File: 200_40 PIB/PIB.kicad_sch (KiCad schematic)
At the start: 160 parts, among them J1 M80-5100442, J11 53398-0271, J12 M80-5100842, J13 53398-0271, J15 53398-0571, J2 53398-0471, J3 G125-MS12605M2P, J5 53398-1371, J6 MMCX, J8 SWD/DEBUG, Q1 Si7489DP, Q11 IRF7832, Q2 Si7489DP, Q9 IRF7832, SW1 B3F-1000, U10 LT8580EDD, U12 MAX823TEUK_T, U14 74HC08PW, U15 74HC08PW, U4 STM32G431RBTx, U5 ADM1270ACPZ, U7 ADM1270ACPZ, Y1 ABM3B-8.000MHZ-10-D1G-T

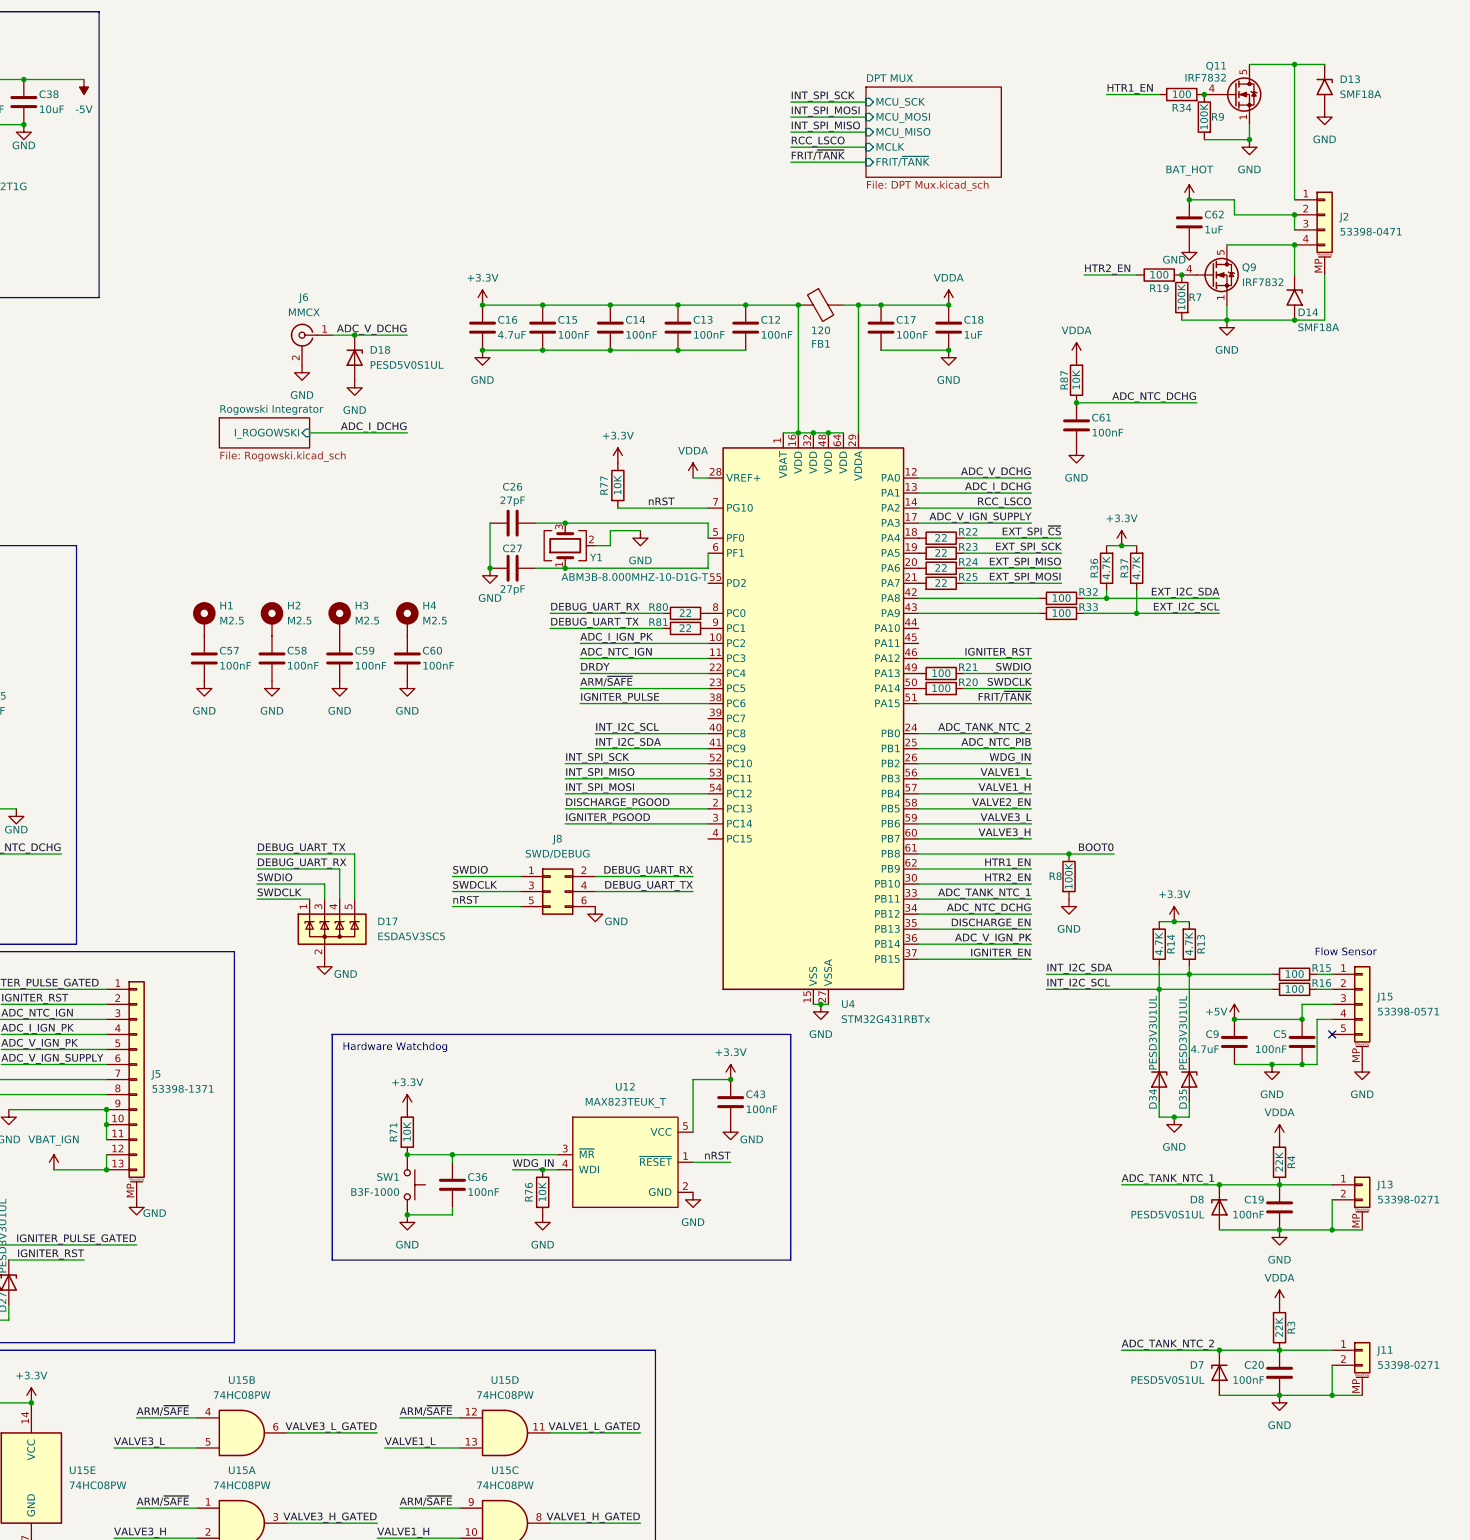
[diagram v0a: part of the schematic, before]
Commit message: clean up schematic
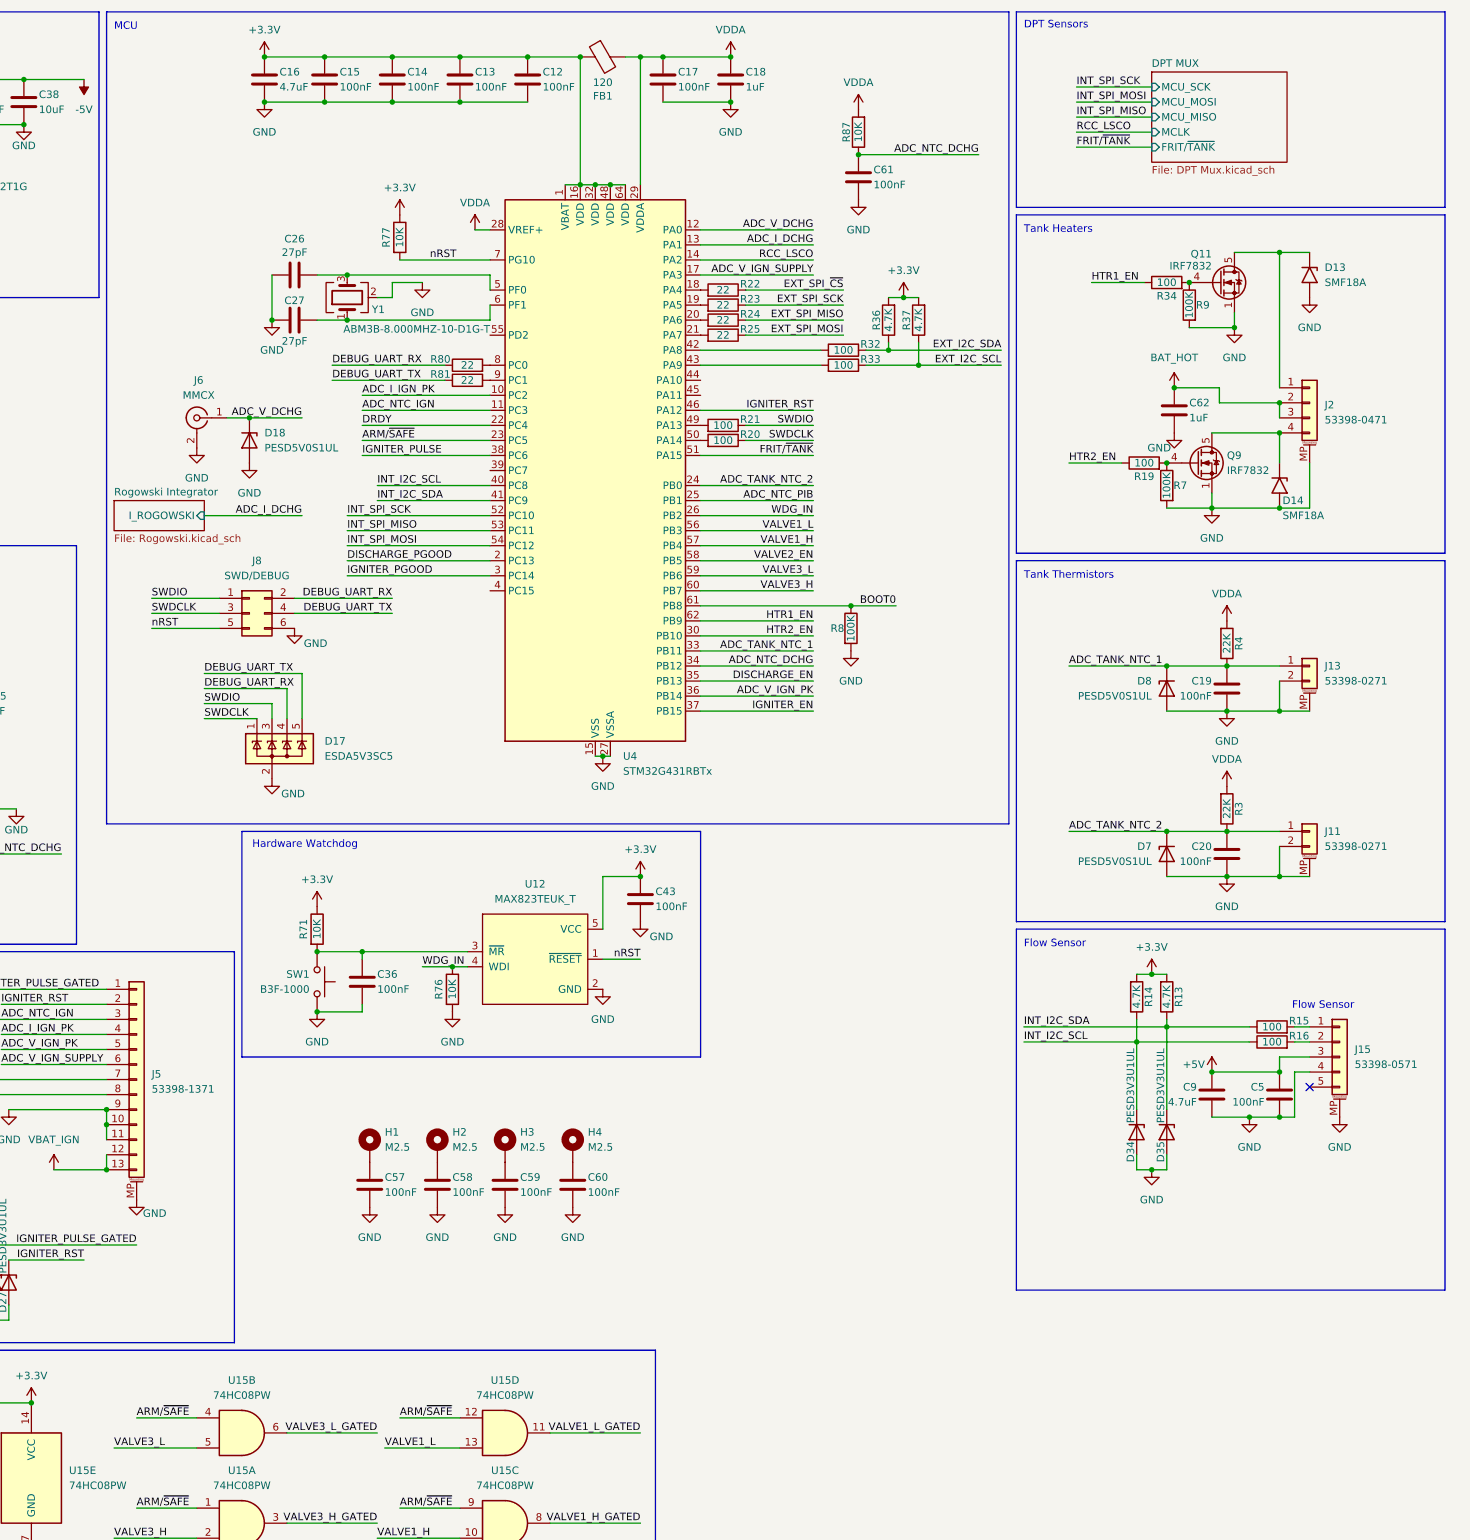
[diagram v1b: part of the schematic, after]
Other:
- note added: "DPT Sensors"
- note added: "MCU"
- note added: "Tank Heaters"
- note added: "Tank Thermistors"
- moved on the sheet: C12, C13, C14, C15, C16, C17, C18, C19, C20, C26, C27, C36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

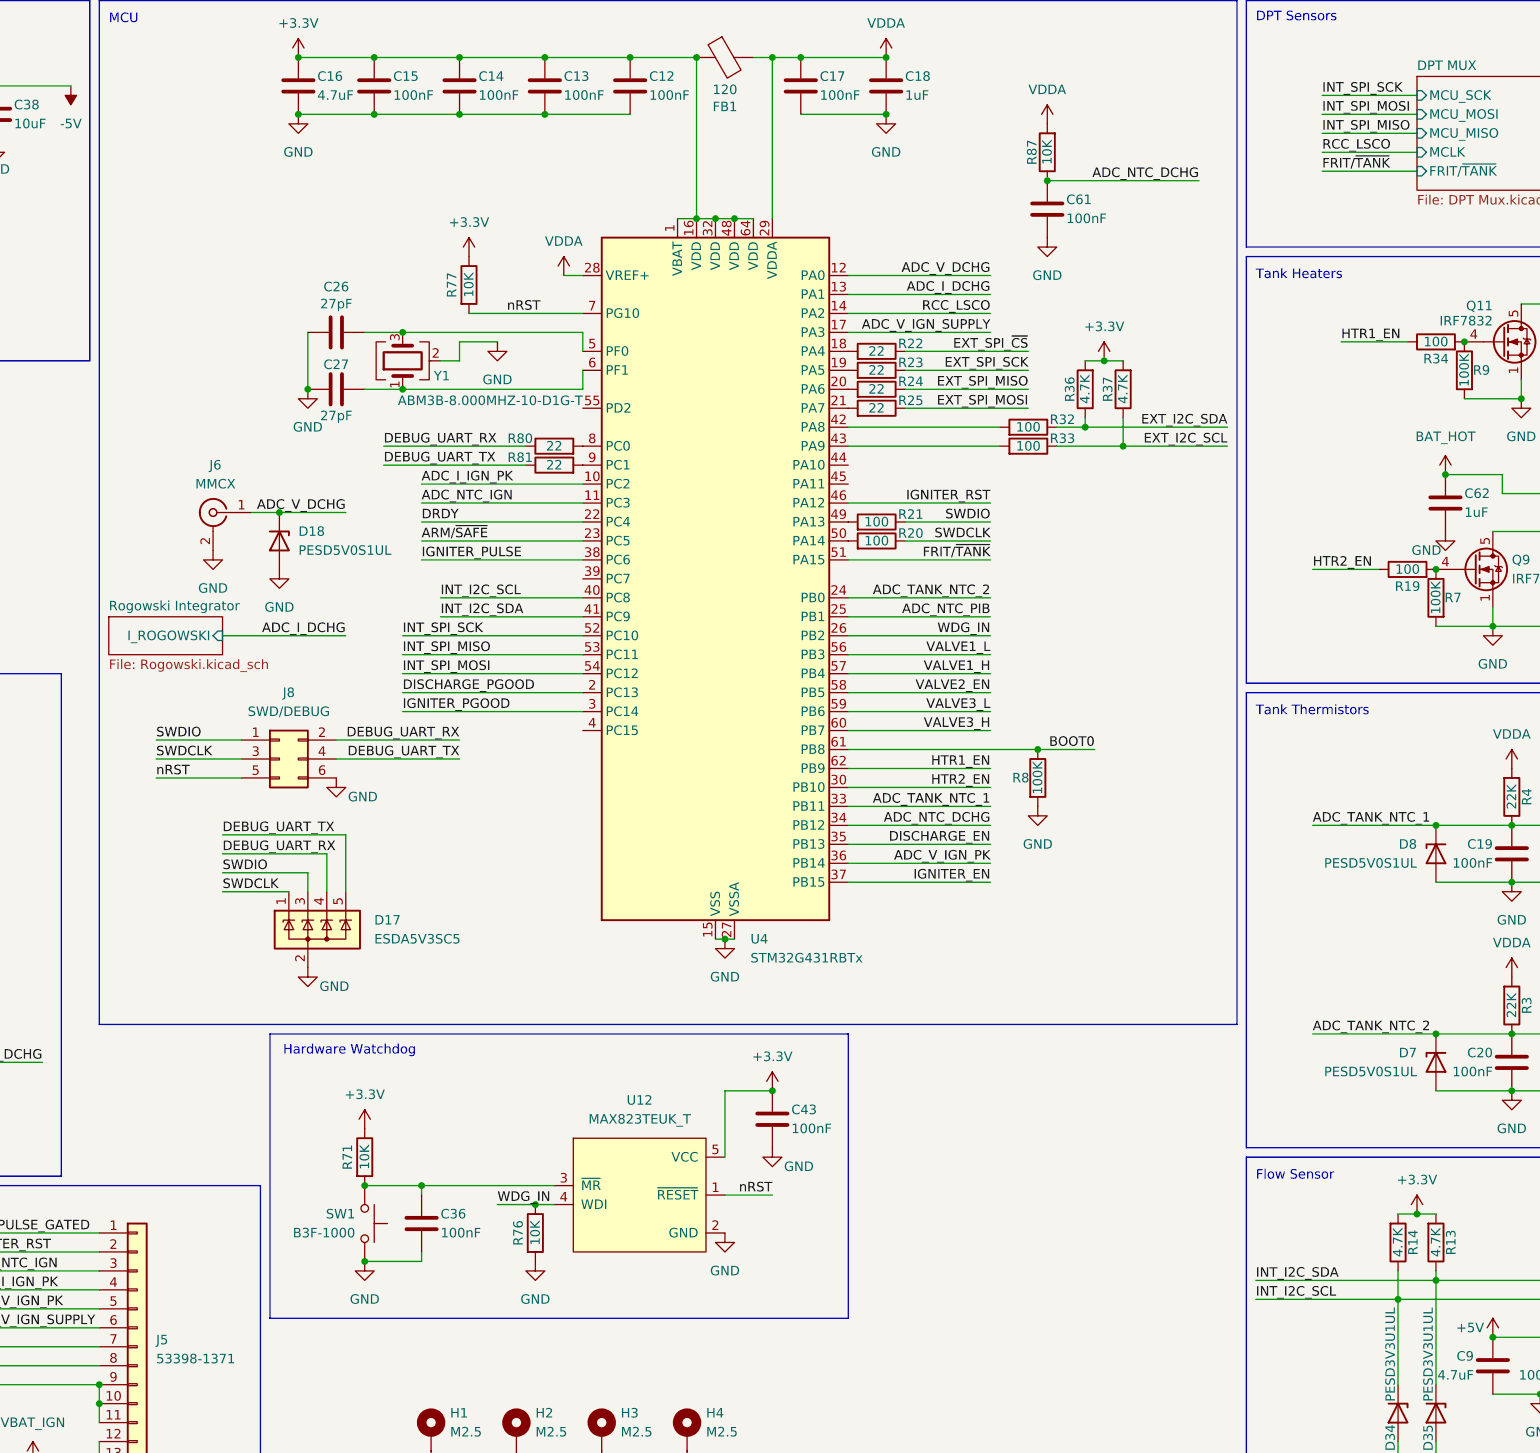
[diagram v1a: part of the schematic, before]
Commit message: fix GSE valve having no power path, fix arm/safe gate floating on reset, fix resistor OR on GSE NC valve, add NC valve flyback diode, change DPT MCLK source to a timer off of HSE, fix crystal load capacitances
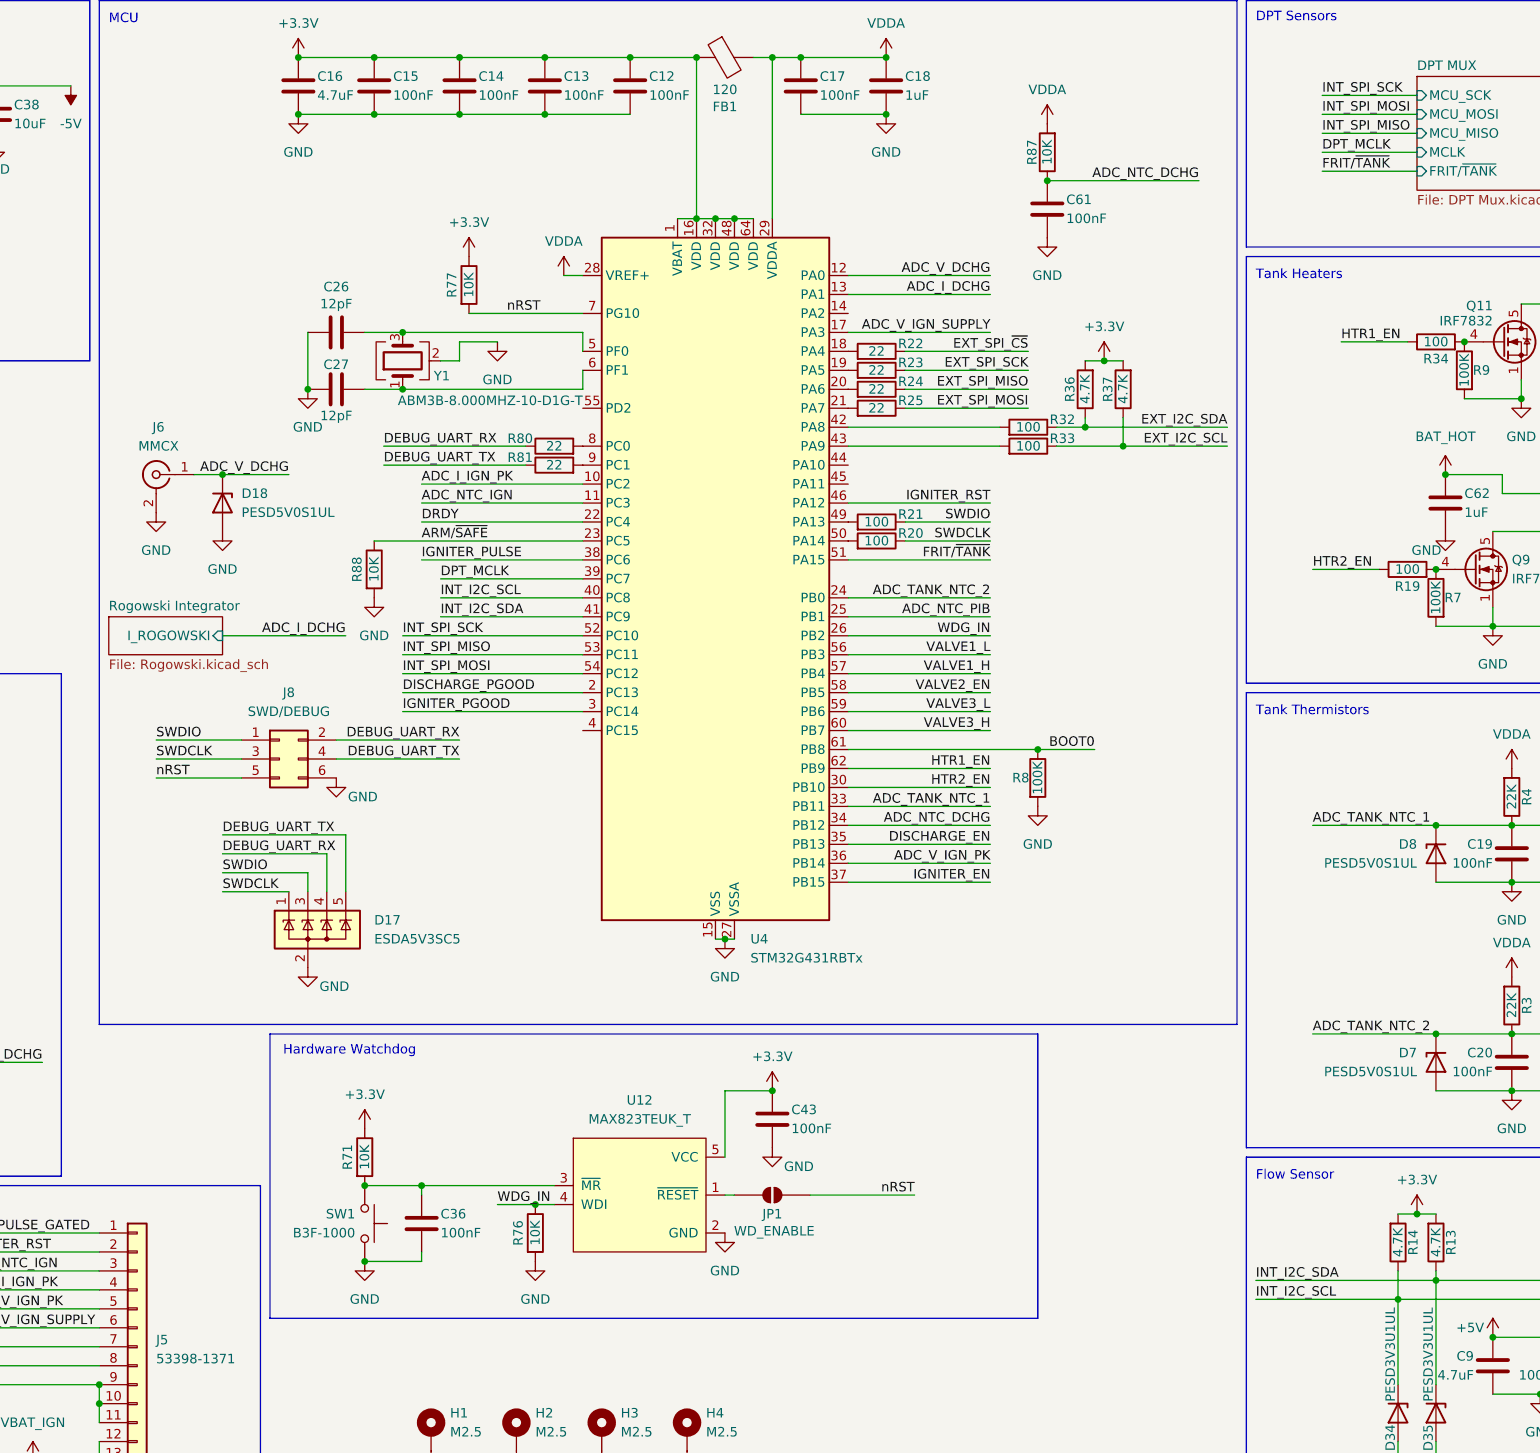
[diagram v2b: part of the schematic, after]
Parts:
- added JP1: WD_ENABLE, Jumper:SolderJumper-2_P1.3mm_Open_Pad1.0x1.5mm, symbol Jumper:SolderJumper_2_Open
- added R88: 10K, Resistor_SMD:R_0402_1005Metric, symbol Device:R
- C26, C27: value 27pF -> 12pF
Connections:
- net ARM/~{SAFE}: now also R88.1
- net GND: now also R88.2
- net nRST: now also JP1.2 (B); no longer U12.1 (~{RESET})
- net DPT_MCLK: now reaches U4.39 (PC7)
- net RCC_LSCO: no longer names the net of U4.14 (PA2)
- new net: JP1.1 (A), U12.1 (~{RESET})
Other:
- moved on the sheet: D18, J6

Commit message: clear out claude flagged items
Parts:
- removed D18: PESD5V0S1UL, Diode_SMD:D_SOD-882, symbol Diode:PESD5V0S1UL
- removed J6: MMCX, Connector_Coaxial:MMCX_Molex_73415-1471_Vertical, symbol Connector:Conn_Coaxial
- added C76, C77: 100nF, Capacitor_SMD:C_0402_1005Metric, symbol Device:C
- added D18: LED, LED_SMD:LED_0603_1608Metric, symbol Device:LED
- added D45, D46, D49: PESD3V3U1UL, Diode_SMD:D_SOD-882, symbol Diode:PESD3V3U1UL
- added R103, R108: 1K, Resistor_SMD:R_0402_1005Metric, symbol Device:R
- added R109: 10K, Resistor_SMD:R_0402_1005Metric, symbol Device:R
- added TH1: 3435K 10K, Resistor_SMD:R_0603_1608Metric, symbol Device:Thermistor_NTC
- added U8: 74AHC1G125, Package_TO_SOT_SMD:SOT-23-5, symbol 74xGxx:74AHC1G125
- SW1: value B3F-1000 -> SKRKAHE020; footprint Button_Switch_THT:SW_PUSH_6mm -> Button_Switch_SMD:SW_Push_SPST_NO_Alps_SKRK
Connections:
- net +3.3V: now also C77.1, R108.1, U8.5 (VCC)
- net ADC_NTC_PIB: now also C76.1, R109.1, TH1.1
- net GND: now also SW1.2, C76.2, C77.2, D18.1 (K), D45.2 (A), D46.2 (A), D49.2 (A), TH1.2, U8.1, U8.3 (GND); no longer SW1.1
- net IGNITER_PULSE_GATED: now also U8.2; no longer R29.1
- net IGNITER_RST: no longer J5.2 (Pin_2), U4.46 (PA12)
- net VDDA: now also R109.2
- net WDG_IN: now also JP1.1 (A); no longer U12.4 (WDI)
- net nRST: now also U12.1 (~{RESET}); no longer J8.5 (Pin_5), JP1.2 (B)
- net at C36.1, R71.2, U12.3 (~{MR}): now also SW1.1; no longer SW1.2
- net at J3.22 (Pin_22), R29.2: now also D45.1 (K)
- net at J3.23 (Pin_23), R30.2: now also D46.1 (K)
- net at J3.24 (Pin_24), R31.2: now also D49.1 (K)
- net DEBUG_LED: now reaches U4.55 (PD2)
- net DEBUG_LED: now also R103.1
- new net: D18.2 (A), R103.2
- new net: JP1.2 (B), U12.4 (WDI)
- new net: J8.5 (Pin_5), R108.2
- new net IGNITER_EXT: R29.1, U8.4
- new net PD_RST: J5.2 (Pin_2), U4.46 (PA12)
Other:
- sheet Rogowski Integrator ports: added ROGOWSKI_RST, V_DISCHARGE; removed none
- note added: "Igniter Buffer"
- moved on the sheet: C43, D2, D3, D9, R29, R30, R31, U12

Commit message: clod
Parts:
- C29, C34: value 10nF -> 100nF
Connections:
- net PD_RST is gone; now on net ~{PD_RST}: J5.2 (Pin_2), U4.46 (PA12)
- net IGNITER_RST renamed ~{PD_RST}
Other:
- sheet Rogowski Integrator ports: added ~{ROGOWSKI_RST}; removed ROGOWSKI_RST
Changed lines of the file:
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@@
 		)
 	)
-	(label "PD_RST"
+	(label "~{PD_RST}"
 		(at 298.45 80.01 180)
 		(effects
@@
 		)
 	)
-	(label "PD_RST"
+	(label "~{PD_RST}"
 		(at 161.29 180.34 0)
 		(effects
@@
 		)
 	)
-	(label "IGNITER_RST"
+	(label "~{PD_RST}"
 		(at 175.26 223.52 180)
 		(effects
@@
 		)
 	)
-	(label "PD_RST"
+	(label "~{PD_RST}"
 		(at 213.36 81.28 180)
 		(effects
@@
 			)
 		)
-		(property "Value" "10nF"
+		(property "Value" "100nF"
 			(at 93.98 226.06 0)
 			(show_name no)
@@
 			)
 		)
-		(property "Value" "10nF"
+		(property "Value" "100nF"
 			(at 93.98 157.48 0)
 			(show_name no)
@@
 			)
 		)
-		(pin "I_ROGOWSKI" input
-			(at 200.66 76.2 0)
+		(pin "V_DISCHARGE" output
+			(at 200.66 78.74 0)
 			(effects
 				(font
@@
 			)
 		)
-		(pin "ROGOWSKI_RST" input
-			(at 200.66 81.28 0)
+		(pin "I_ROGOWSKI" output
+			(at 200.66 76.2 0)
 			(effects
 				(font
@@
 			)
 		)
-		(pin "V_DISCHARGE" input
-			(at 200.66 78.74 0)
+		(pin "~{ROGOWSKI_RST}" input
+			(at 200.66 81.28 0)
 			(effects
 				(font
